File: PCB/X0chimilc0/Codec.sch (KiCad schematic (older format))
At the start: 1 part

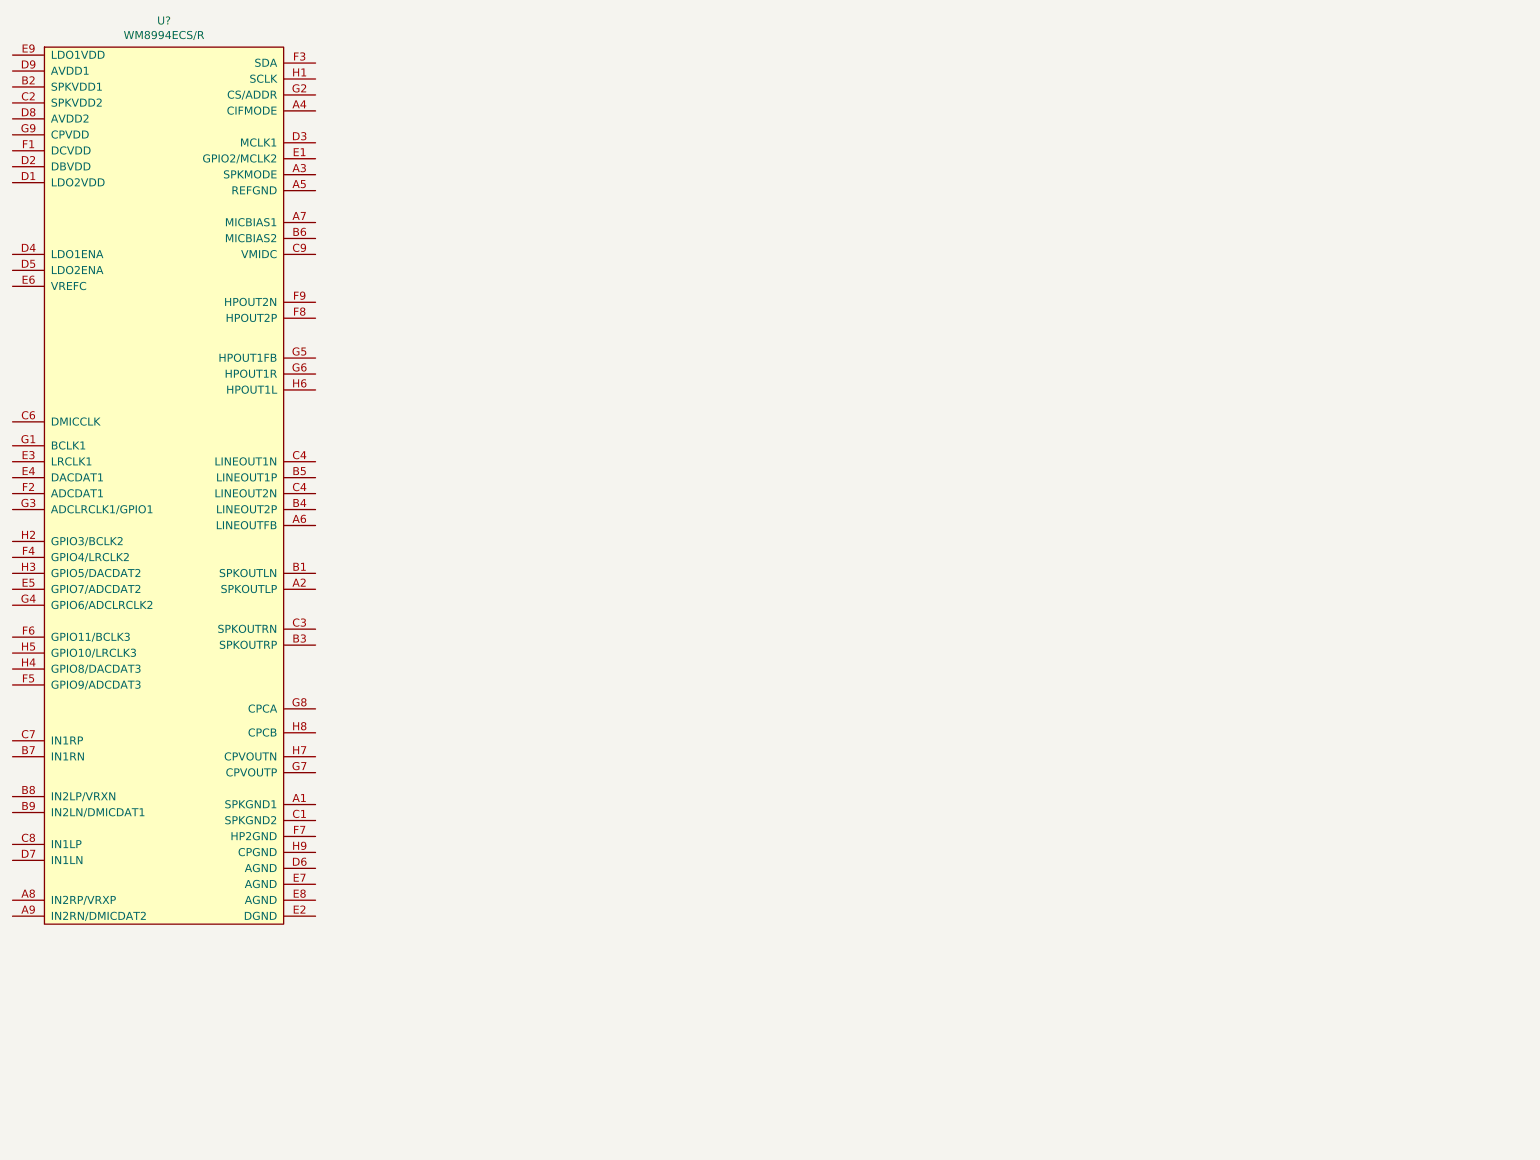
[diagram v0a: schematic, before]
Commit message: PCB Mockup
Made components for DAC/MCU/FPGA/Connectors, mocked things up as PCB, going to be crazy.
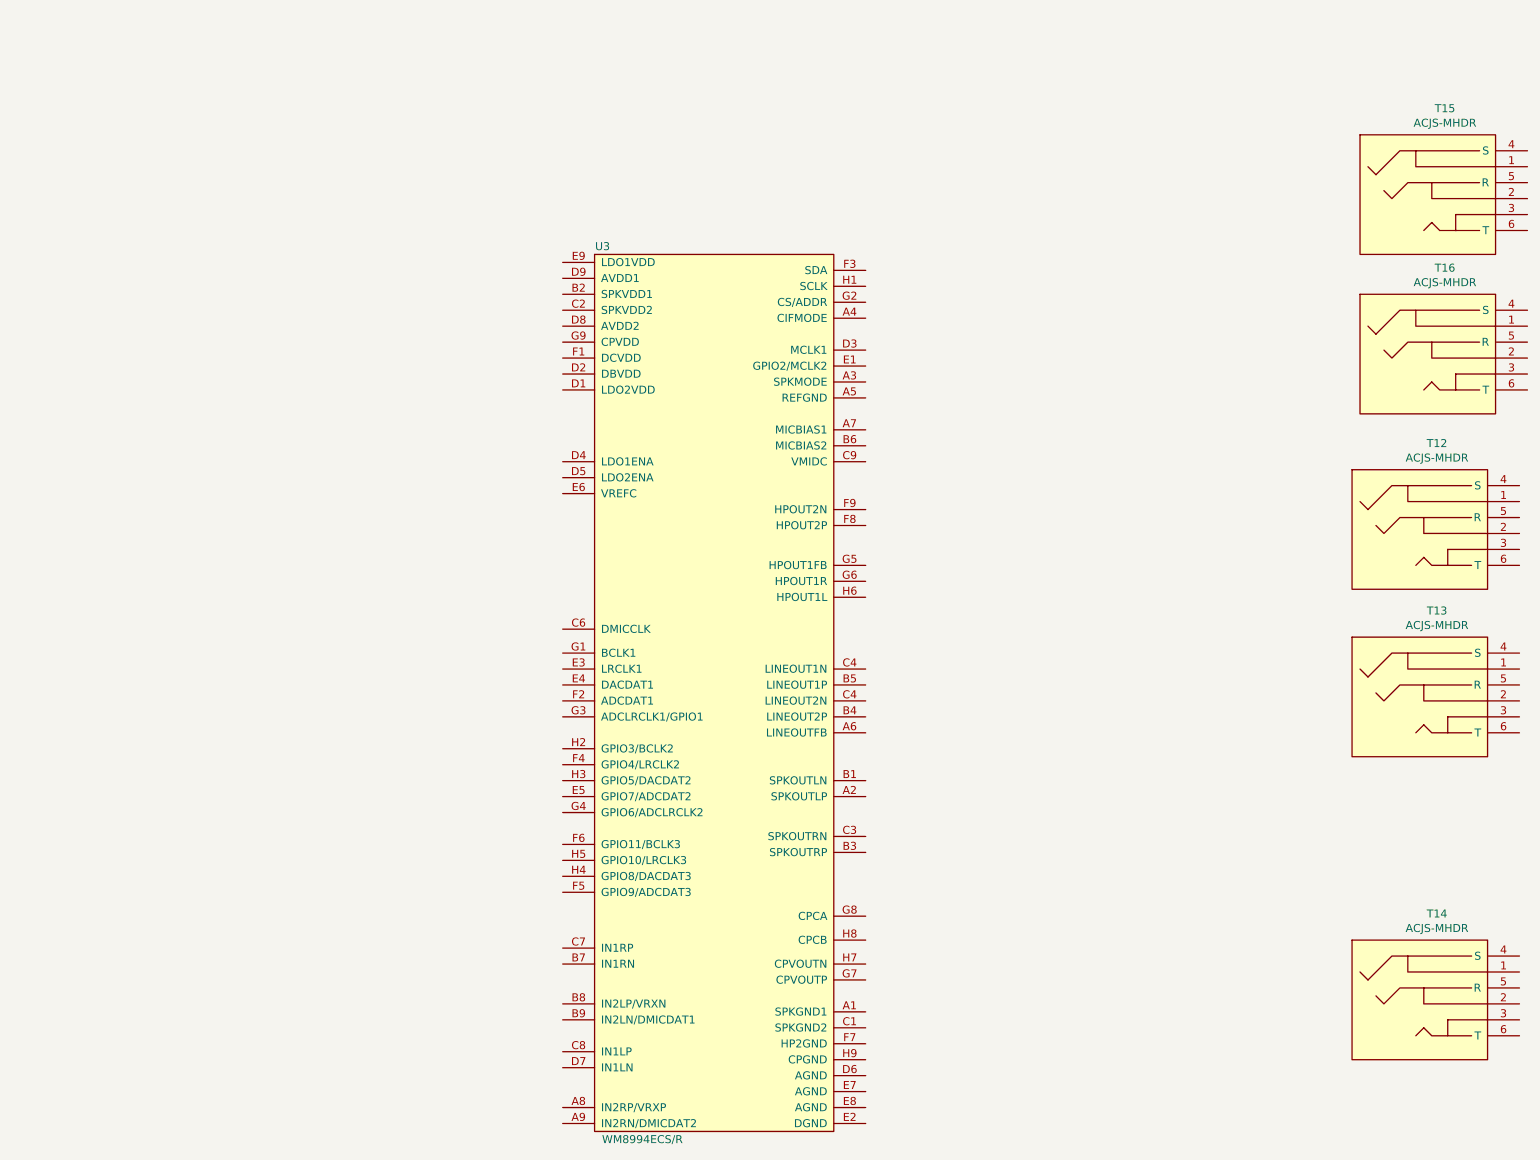
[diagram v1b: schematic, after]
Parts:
- added T12, T13, T14, T15, T16: ACJS-MHDR, AVR-KiCAD-Lib-Connectors:ACJS-MHDR, symbol AVR-KiCAD-Lib-Connectors:ACJS-MHDR
- gave numbers to parts that had none: 1
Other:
- moved on the sheet: U3

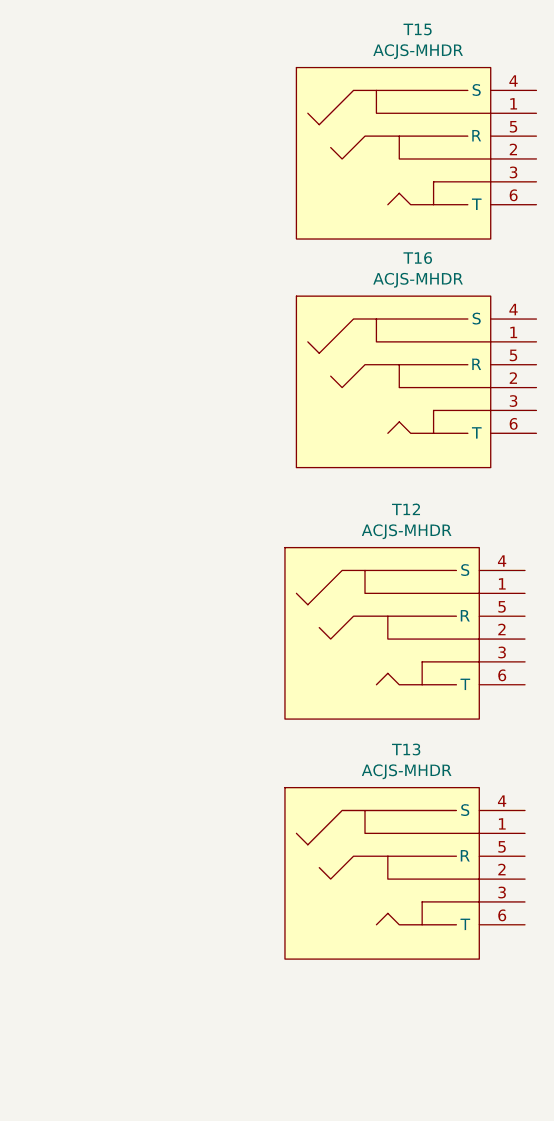
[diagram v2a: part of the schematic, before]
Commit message: Component PDFs
added relevant PDF datasheets and some minor schematic edits
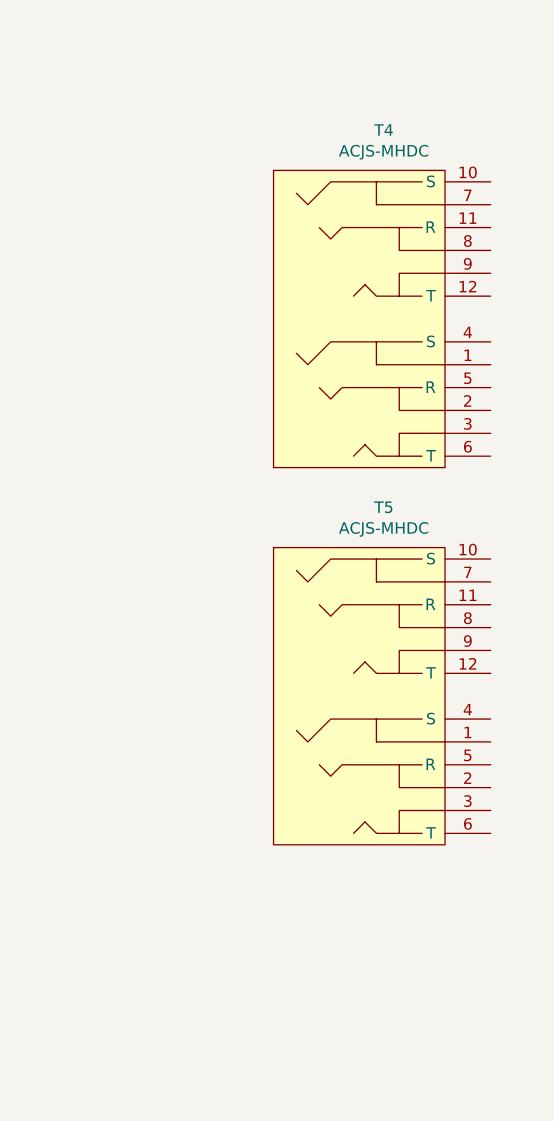
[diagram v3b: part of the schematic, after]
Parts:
- removed T12, T13, T15, T16: ACJS-MHDR, AVR-KiCAD-Lib-Connectors:ACJS-MHDR, symbol AVR-KiCAD-Lib-Connectors:ACJS-MHDR
- added T4, T5: ACJS-MHDC, AVR-KiCAD-Lib-Connectors:ACJS-MHDC, symbol AVR-KiCAD-Lib-Connectors:ACJS-MHDC

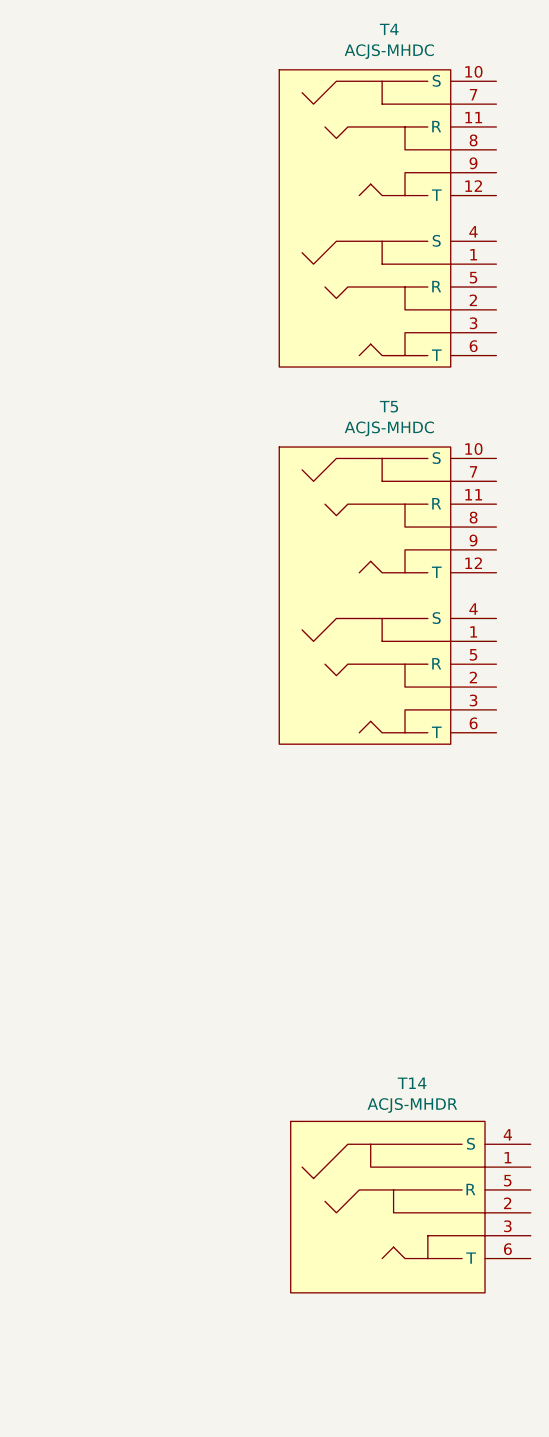
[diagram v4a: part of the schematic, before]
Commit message: USB
USB C page of schematics first pass complete
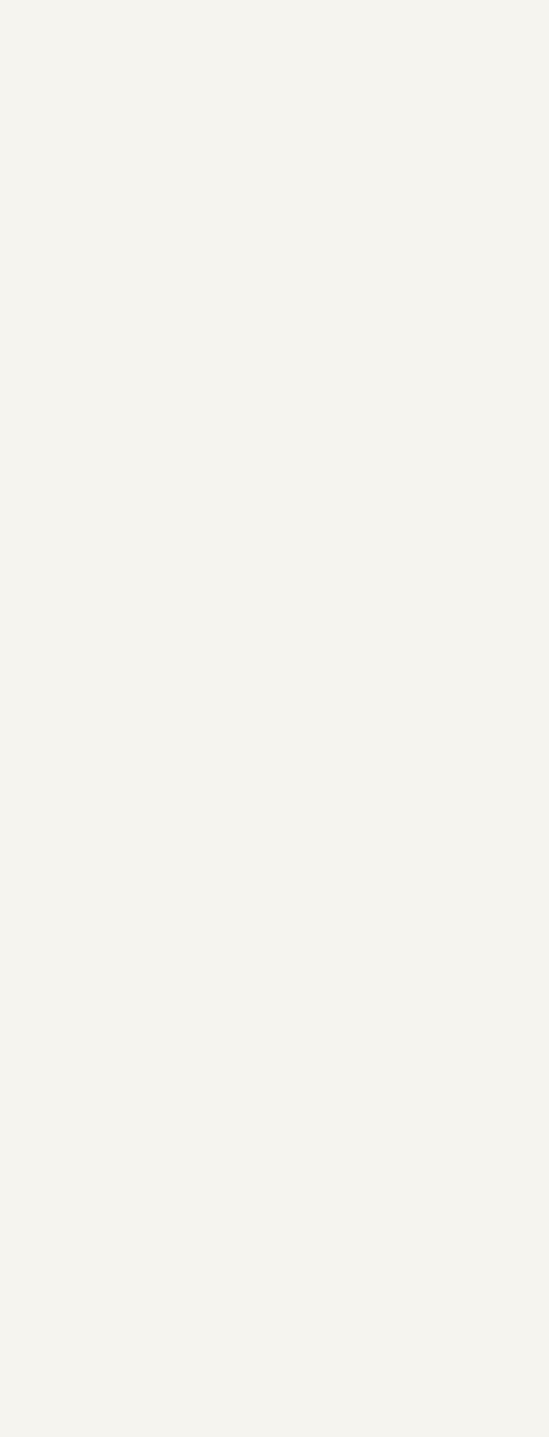
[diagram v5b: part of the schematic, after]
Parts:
- removed T14: ACJS-MHDR, AVR-KiCAD-Lib-Connectors:ACJS-MHDR, symbol AVR-KiCAD-Lib-Connectors:ACJS-MHDR
- removed T4, T5: ACJS-MHDC, AVR-KiCAD-Lib-Connectors:ACJS-MHDC, symbol AVR-KiCAD-Lib-Connectors:ACJS-MHDC
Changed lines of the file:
@@
 $Descr A3 16535 11693
 encoding utf-8
-Sheet 7 8
+Sheet 7 10
 Title ""
 Date ""
@@
 	1    0    0    -1
 $EndComp
-$Comp
-L AVR-KiCAD-Lib-Connectors:ACJS-MHDR T14
-U 1 1 5E48264F
-P 12450 6800
-F 0 "T14" H 12133 7165 50  0000 C CNN
-F 1 "ACJS-MHDR" H 12133 7074 50  0000 C CNN
-F 2 "AVR-KiCAD-Lib-Connectors:ACJS-MHDR" H 12350 8300 50  0001 C CNN
-F 3 "https://www.amphenol-sine.com/pdf/datasheet/ACJS-MHDR.pdf" H 12450 8400 50  0001 C CNN
-F 4 "1.41000" H 12650 8550 50  0001 C CNN "Cost QTY: 1"
-F 5 "0.81420" H 12750 8650 50  0001 C CNN "Cost QTY: 1000"
-F 6 "0.74520" H 12850 8750 50  0001 C CNN "Cost QTY: 2500"
-F 7 "*" H 12950 8850 50  0001 C CNN "Cost QTY: 5000"
-F 8 "*" H 13050 8950 50  0001 C CNN "Cost QTY: 10000"
-F 9 "Amphenol Sine Systems Corp" H 13150 9050 50  0001 C CNN "MFR"
-F 10 "ACJS-MHDR" H 13250 9150 50  0001 C CNN "MFR#"
-F 11 "Digikey" H 13350 9250 50  0001 C CNN "Vendor"
-F 12 "889-1817-ND" H 13450 9350 50  0001 C CNN "Vendor #"
-F 13 "AVR" H 13550 9450 50  0001 C CNN "Designer"
-F 14 "12.7mm" H 13650 9550 50  0001 C CNN "Height"
-F 15 "1/5/2019" H 14750 10650 50  0001 C CNN "Date Created"
-F 16 "1/5/2019" H 13750 9650 50  0001 C CNN "Date Modified"
-F 17 "Yes" H 13850 9750 50  0001 C CNN "Lead-Free ?"
-F 18 "RoHS 1" H 13950 9850 50  0001 C CNN "RoHS Levels"
-F 19 "ThroughHole" H 14050 9950 50  0001 C CNN "Mounting"
-F 20 "6" H 14150 10050 50  0001 C CNN "Pin Count #"
-F 21 "Active" H 14250 10150 50  0001 C CNN "Status"
-F 22 "*" H 14350 10250 50  0001 C CNN "Tolerance"
-F 23 "TRS Connector 6.35mm" H 14450 10350 50  0001 C CNN "Type"
-F 24 "*" H 14550 10450 50  0001 C CNN "Voltage"
-F 25 "*" H 14650 10600 50  0001 C CNN "Package"
-F 26 "CONN JACK STEREO 1/4\" R/A" H 15050 11000 50  0001 C CNN "Description"
-F 27 "ACJS-MHDR" H 14850 10800 50  0001 C CNN "_Value_"
-F 28 "*" H 14950 10900 50  0001 C CNN "Management_ID"
-	1    12450 6800
-	1    0    0    -1
-$EndComp
-$Comp
-L AVR-KiCAD-Lib-Connectors:ACJS-MHDC T4
-U 1 1 5DF12B1F
-P 12300 2850
-F 0 "T4" H 12033 3875 50  0000 C CNN
-F 1 "ACJS-MHDC" H 12033 3784 50  0000 C CNN
-F 2 "AVR-KiCAD-Lib-Connectors:ACJS-MHDC" H 12100 4400 50  0001 C CNN
-F 3 "http://www.amphenol-sine.com/pdf/datasheet/ACJS-MHDC.pdf" H 12200 4500 50  0001 C CNN
-F 4 "2.83000" H 11650 3850 50  0001 C CNN "Cost QTY: 1"
-F 5 "1.71720" H 11750 3950 50  0001 C CNN "Cost QTY: 1000"
-F 6 "1.61120" H 11850 4050 50  0001 C CNN "Cost QTY: 2500"
-F 7 "*" H 11950 4150 50  0001 C CNN "Cost QTY: 5000"
-F 8 "*" H 12050 4250 50  0001 C CNN "Cost QTY: 10000"
-F 9 "Aphenol Sine Systems Corp" H 12150 4350 50  0001 C CNN "MFR"
-F 10 "ACJS-MHDC" H 12250 4450 50  0001 C CNN "MFR#"
-F 11 "Digikey" H 12350 4550 50  0001 C CNN "Vendor"
-F 12 "889-1816-ND" H 12450 4650 50  0001 C CNN "Vendor #"
-F 13 "AVR" H 12550 4750 50  0001 C CNN "Designer"
-F 14 "29.32mm" H 12650 4850 50  0001 C CNN "Height"
-F 15 "1/1/2019" H 13750 5950 50  0001 C CNN "Date Created"
-F 16 "1/1/2019" H 12750 4950 50  0001 C CNN "Date Modified"
-F 17 "Yes" H 12850 5050 50  0001 C CNN "Lead-Free ?"
-F 18 "RoHS 1" H 12950 5150 50  0001 C CNN "RoHS Levels"
-F 19 "Throughole" H 13050 5250 50  0001 C CNN "Mounting"
-F 20 "12" H 13150 5350 50  0001 C CNN "Pin Count #"
-F 21 "Active" H 13250 5450 50  0001 C CNN "Status"
-F 22 "*" H 13350 5550 50  0001 C CNN "Tolerance"
-F 23 "TRS Stereo Dual Connector " H 13450 5650 50  0001 C CNN "Type"
-F 24 "*" H 13550 5750 50  0001 C CNN "Voltage"
-F 25 "*" H 13650 5900 50  0001 C CNN "Package"
-F 26 "CONN JACK DUAL STEREO 1/4\" R/A" H 14050 6300 50  0001 C CNN "Description"
-F 27 "ACJS-MHDC" H 13850 6100 50  0001 C CNN "_Value_"
-F 28 "*" H 13950 6200 50  0001 C CNN "Management_ID"
-	1    12300 2850
-	1    0    0    -1
-$EndComp
-$Comp
-L AVR-KiCAD-Lib-Connectors:ACJS-MHDC T5
-U 1 1 5DF1777E
-P 12300 4500
-F 0 "T5" H 12033 5525 50  0000 C CNN
-F 1 "ACJS-MHDC" H 12033 5434 50  0000 C CNN
-F 2 "AVR-KiCAD-Lib-Connectors:ACJS-MHDC" H 12100 6050 50  0001 C CNN
-F 3 "http://www.amphenol-sine.com/pdf/datasheet/ACJS-MHDC.pdf" H 12200 6150 50  0001 C CNN
-F 4 "2.83000" H 11650 5500 50  0001 C CNN "Cost QTY: 1"
-F 5 "1.71720" H 11750 5600 50  0001 C CNN "Cost QTY: 1000"
-F 6 "1.61120" H 11850 5700 50  0001 C CNN "Cost QTY: 2500"
-F 7 "*" H 11950 5800 50  0001 C CNN "Cost QTY: 5000"
-F 8 "*" H 12050 5900 50  0001 C CNN "Cost QTY: 10000"
-F 9 "Aphenol Sine Systems Corp" H 12150 6000 50  0001 C CNN "MFR"
-F 10 "ACJS-MHDC" H 12250 6100 50  0001 C CNN "MFR#"
-F 11 "Digikey" H 12350 6200 50  0001 C CNN "Vendor"
-F 12 "889-1816-ND" H 12450 6300 50  0001 C CNN "Vendor #"
-F 13 "AVR" H 12550 6400 50  0001 C CNN "Designer"
-F 14 "29.32mm" H 12650 6500 50  0001 C CNN "Height"
-F 15 "1/1/2019" H 13750 7600 50  0001 C CNN "Date Created"
-F 16 "1/1/2019" H 12750 6600 50  0001 C CNN "Date Modified"
-F 17 "Yes" H 12850 6700 50  0001 C CNN "Lead-Free ?"
-F 18 "RoHS 1" H 12950 6800 50  0001 C CNN "RoHS Levels"
-F 19 "Throughole" H 13050 6900 50  0001 C CNN "Mounting"
-F 20 "12" H 13150 7000 50  0001 C CNN "Pin Count #"
-F 21 "Active" H 13250 7100 50  0001 C CNN "Status"
-F 22 "*" H 13350 7200 50  0001 C CNN "Tolerance"
-F 23 "TRS Stereo Dual Connector " H 13450 7300 50  0001 C CNN "Type"
-F 24 "*" H 13550 7400 50  0001 C CNN "Voltage"
-F 25 "*" H 13650 7550 50  0001 C CNN "Package"
-F 26 "CONN JACK DUAL STEREO 1/4\" R/A" H 14050 7950 50  0001 C CNN "Description"
-F 27 "ACJS-MHDC" H 13850 7750 50  0001 C CNN "_Value_"
-F 28 "*" H 13950 7850 50  0001 C CNN "Management_ID"
-	1    12300 4500
-	1    0    0    -1
-$EndComp
